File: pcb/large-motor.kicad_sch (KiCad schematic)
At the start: 15 parts, among them J6 Screw_Terminal_01x02, U27 DRV8874PWPR

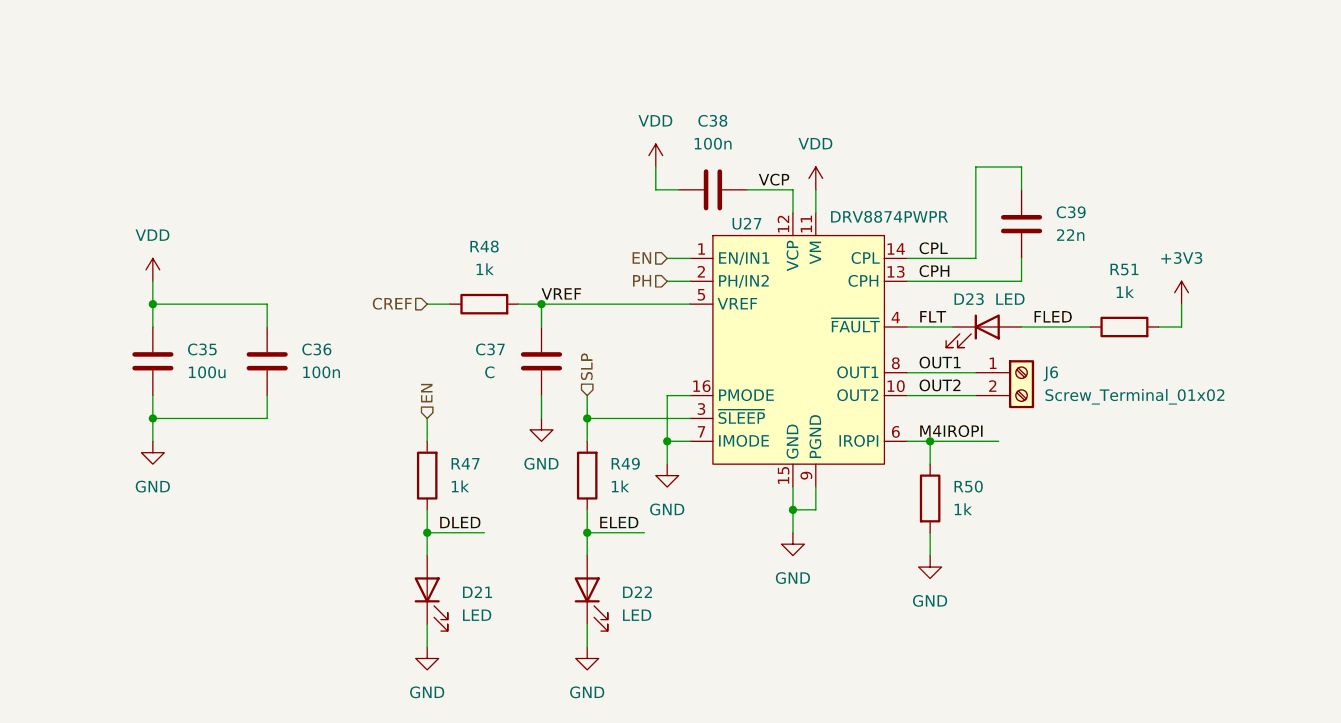
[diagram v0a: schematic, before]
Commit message: Remove sensor hub
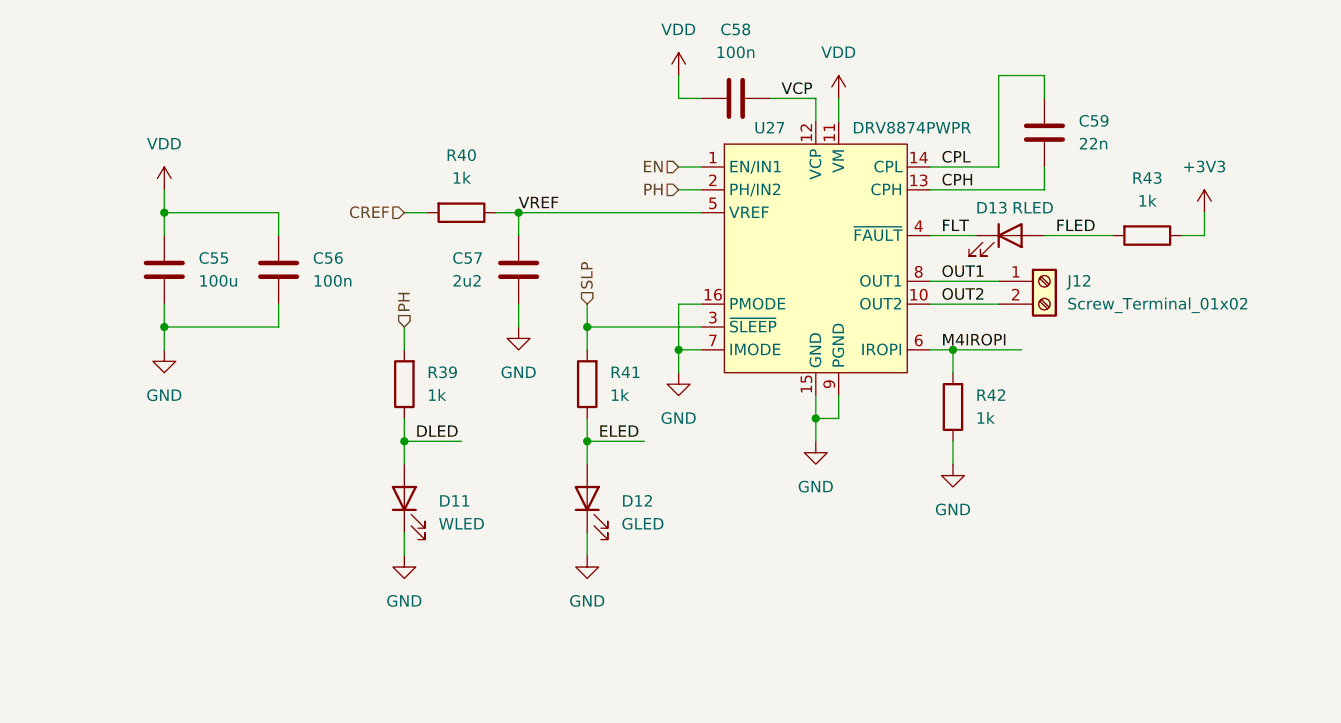
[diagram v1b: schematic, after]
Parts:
- removed R48, R49, R50, R51: 1k, symbol Device:R
- added R40, R41, R42, R43: 1k, Resistor_SMD:R_0402_1005Metric, symbol Device:R
- C57: renamed from C37; value C -> 2u2; LCSC (none) -> C12530
- C58: renamed from C38; LCSC (none) -> C307331
- C59: renamed from C39; LCSC (none) -> C1532
- D11: renamed from D21; value LED -> WLED; footprint (none) -> LED_SMD:LED_0603_1608Metric; LCSC (none) -> C2290
- D12: renamed from D22; value LED -> GLED; footprint (none) -> LED_SMD:LED_0603_1608Metric; LCSC (none) -> C72043
- D13: renamed from D23; value LED -> RLED; footprint (none) -> LED_SMD:LED_0603_1608Metric; LCSC (none) -> C2286
- J12: renamed from J6; footprint (none) -> TerminalBlock_Phoenix:TerminalBlock_Phoenix_MKDS-1,5-2_1x02_P5.00mm_Horizontal; LCSC (none) -> C8404
- R39: renamed from R47; footprint (none) -> Resistor_SMD:R_0402_1005Metric; LCSC (none) -> C11702
- U27: LCSC (none) -> C1855818
- renumbered C35 to C55, C36 to C56
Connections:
- net +3V3: now also R43.1
- net CREF: now also R40.2
- net ELED: now also R41.1
- net EN: no longer R39.2
- net FLED: now also R43.2
- net GND: now also R42.1
- net M4IROPI: now also R42.2
- net PH: now also R39.2
- net SLP: now also R41.2
- net VREF: now also R40.1
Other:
- moved on the sheet: C55, C56, C57, C58, C59, D11, D12, D13, J12, R39, U27

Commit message: Finish schematic
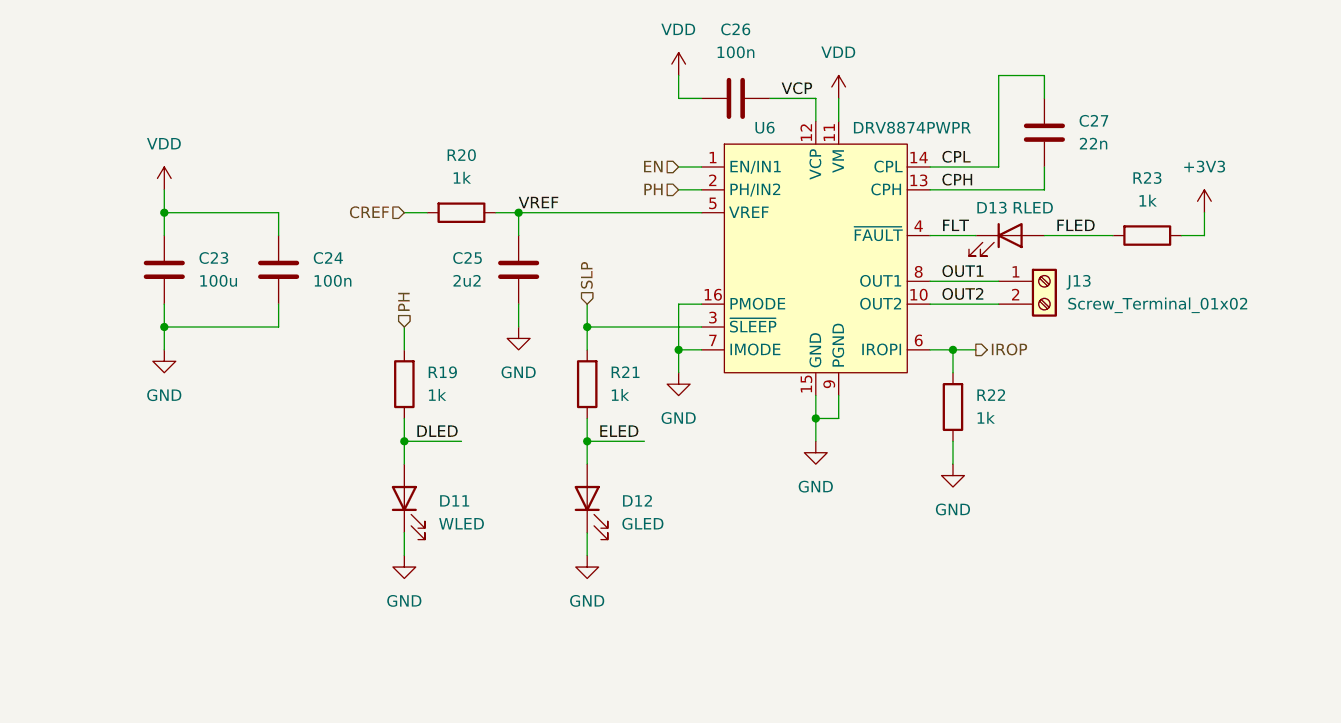
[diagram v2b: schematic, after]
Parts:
- renumbered C55 to C23, C56 to C24, C57 to C25, C58 to C26, C59 to C27, J12 to J13, R39 to R19, R40 to R20, R41 to R21, R42 to R22, R43 to R23, U27 to U6
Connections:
- net M4IROPI renamed IROP

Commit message: Save progress
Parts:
- removed C23: 100u, Capacitor_SMD:C_Elec_8x6.2, symbol Device:C
- removed J13: Screw_Terminal_01x02, TerminalBlock_Phoenix:TerminalBlock_Phoenix_MKDS-1,5-2_1x02_P5.00mm_Horizontal, symbol Connector:Screw_Terminal_01x02
- renumbered C24 to C66, C25 to C67, C26 to C68, C27 to C69, D11 to D26, D12 to D27, D13 to D28, R19 to R59, R20 to R60, R21 to R61, R22 to R62, R23 to R63, U6 to U30
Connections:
- net OUT1 renamed OUTA
- net OUT2 renamed OUTB

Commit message: Save progress
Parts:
- added C13, C57: 22u, Capacitor_SMD:C_0805_2012Metric, symbol Device:C
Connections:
- net GND: now also C13.2, C57.2
- net VDD: now also C13.1, C57.1

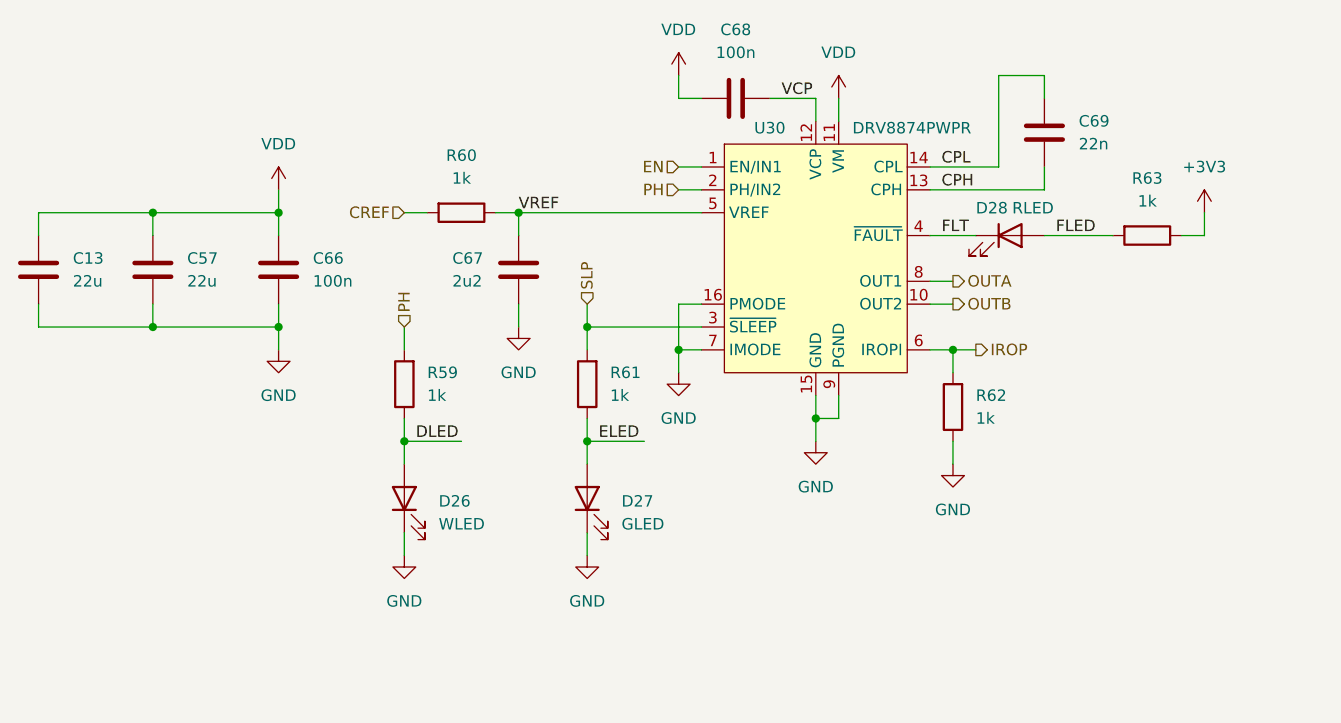
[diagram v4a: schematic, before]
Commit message: Finish schematic
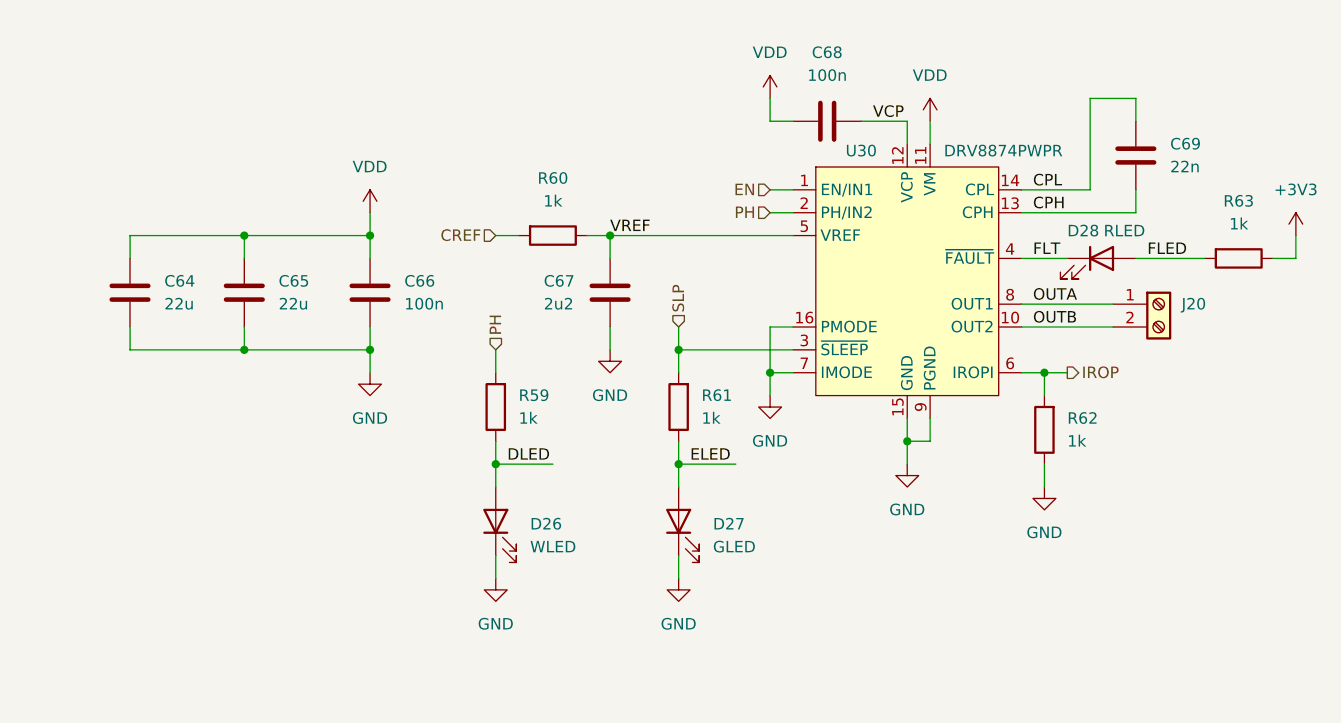
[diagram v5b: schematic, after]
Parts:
- added J20: Screw_Terminal_01x02, TerminalBlock_Phoenix:TerminalBlock_Phoenix_MKDS-1,5-2_1x02_P5.00mm_Horizontal, symbol Connector:Screw_Terminal_01x02
- renumbered C13 to C64, C57 to C65
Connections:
- net OUTA: now also J20.1 (Pin_1)
- net OUTB: now also J20.2 (Pin_2)
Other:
- moved on the sheet: C64, C65, C66, C67, C68, C69, D26, D27, D28, R59, R60, R61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

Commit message: Start wiring
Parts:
- renumbered J20 to J29
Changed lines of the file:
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@@
 		(dnp no)
 		(fields_autoplaced yes)
-		(property "Reference" "J20"
+		(property "Reference" "J29"
 			(at 152.4 58.4199 0)
 			(effects

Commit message: Add power switch
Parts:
- J29: now not fitted
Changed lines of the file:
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@@
 		(in_bom yes)
 		(on_board yes)
-		(dnp no)
+		(dnp yes)
 		(fields_autoplaced yes)
 		(property "Reference" "J29"

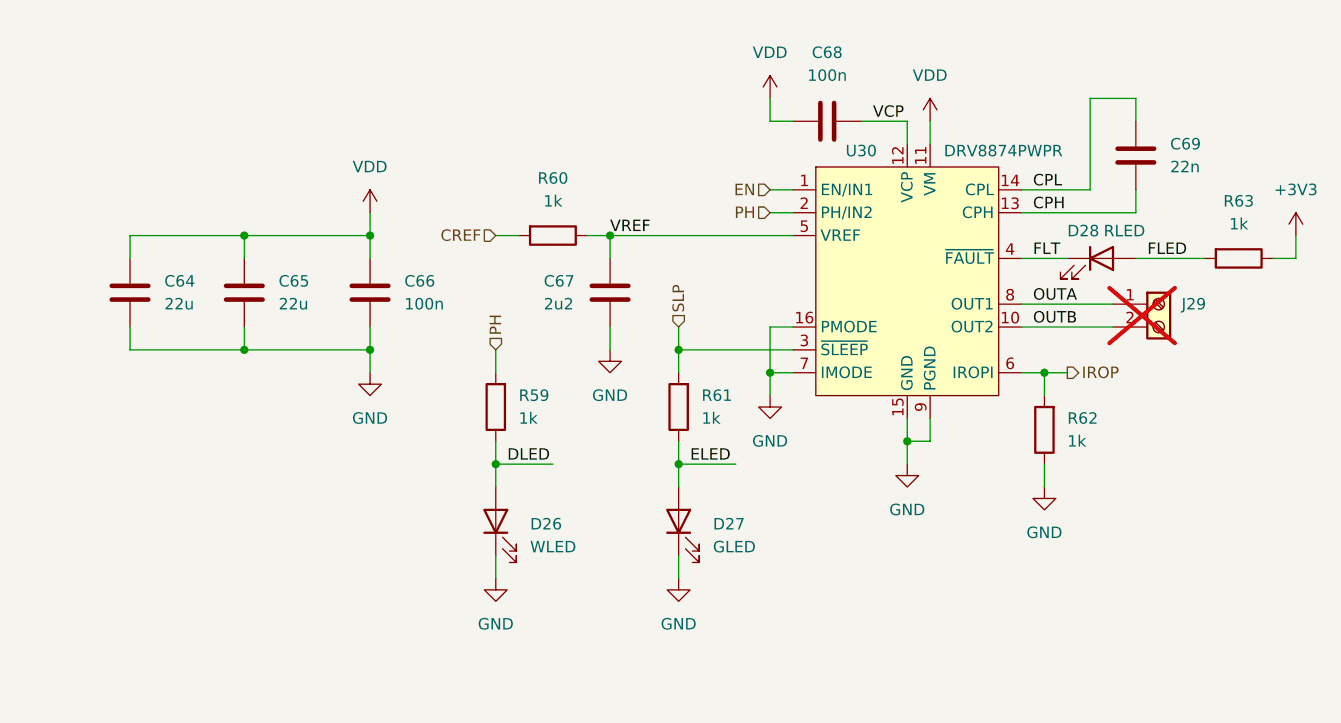
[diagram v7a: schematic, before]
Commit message: Fix encoder pull downs
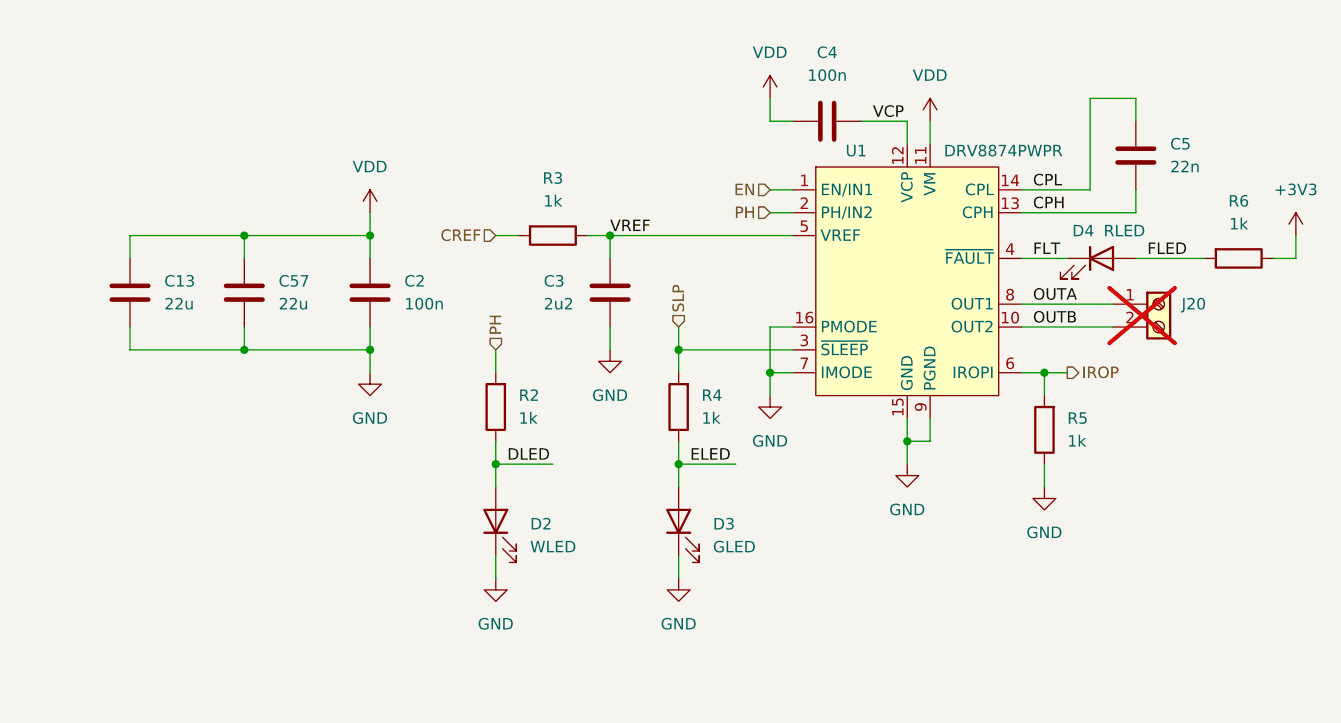
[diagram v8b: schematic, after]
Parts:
- renumbered C64 to C13, C66 to C2, C67 to C3, C68 to C4, C69 to C5, C65 to C57, D26 to D2, D27 to D3, D28 to D4, J29 to J20, R59 to R2, R60 to R3, R61 to R4, R62 to R5, R63 to R6, U30 to U1
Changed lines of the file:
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@@
 (kicad_sch
-	(version 20231120)
+	(version 20250114)
 	(generator "eeschema")
-	(generator_version "8.0")
+	(generator_version "9.0")
 	(paper "A5")
 	(junction
@@
 	(label "CPH"
 		(at 135.89 48.26 0)
-		(fields_autoplaced yes)
 		(effects
 			(font
@@
 	(label "OUTB"
 		(at 135.89 60.96 0)
-		(fields_autoplaced yes)
 		(effects
 			(font
@@
 	(label "CPL"
 		(at 135.89 45.72 0)
-		(fields_autoplaced yes)
 		(effects
 			(font
@@
 	(label "VCP"
 		(at 118.11 38.1 0)
-		(fields_autoplaced yes)
 		(effects
 			(font
@@
 	(label "OUTA"
 		(at 135.89 58.42 0)
-		(fields_autoplaced yes)
 		(effects
 			(font
@@
 	(label "FLED"
 		(at 148.59 53.34 0)
-		(fields_autoplaced yes)
 		(effects
 			(font
@@
 	(label "ELED"
 		(at 97.79 76.2 0)
-		(fields_autoplaced yes)
 		(effects
 			(font
@@
 	(label "VREF"
 		(at 88.9 50.8 0)
-		(fields_autoplaced yes)
 		(effects
 			(font
@@
 	(label "DLED"
 		(at 77.47 76.2 0)
-		(fields_autoplaced yes)
 		(effects
 			(font
@@
 	(label "FLT"
 		(at 135.89 53.34 0)
-		(fields_autoplaced yes)
 		(effects
 			(font
@@
 		(shape input)
 		(at 76.2 50.8 180)
-		(fields_autoplaced yes)
 		(effects
 			(font
@@
 		(shape input)
 		(at 96.52 60.96 90)
-		(fields_autoplaced yes)
 		(effects
 			(font
@@
 		(shape input)
 		(at 106.68 48.26 180)
-		(fields_autoplaced yes)
 		(effects
 			(font
@@
 		(shape input)
 		(at 106.68 45.72 180)
-		(fields_autoplaced yes)
 		(effects
 			(font
@@
 		(shape output)
 		(at 139.7 66.04 0)
-		(fields_autoplaced yes)
 		(effects
 			(font
@@
 		(shape input)
 		(at 76.2 63.5 90)
-		(fields_autoplaced yes)
 		(effects
 			(font
@@
 		(dnp no)
 		(fields_autoplaced yes)
-		(property "Reference" "D27"
+		(property "Reference" "D3"
 			(at 100.33 82.8674 90)
 			(effects
@@
 		(dnp no)
 		(fields_autoplaced yes)
-		(property "Reference" "R60"
+		(property "Reference" "R3"
 			(at 82.55 44.45 90)
 			(effects
@@
 		(dnp no)
 		(fields_autoplaced yes)
-		(property "Reference" "#PWR0242"
+		(property "Reference" "#PWR016"
 			(at 88.9 69.85 0)
 			(effects
@@
 		(on_board yes)
 		(dnp no)
-		(property "Reference" "D28"
+		(property "Reference" "D4"
 			(at 141.478 50.292 0)
 			(effects
@@
 		(dnp yes)
 		(fields_autoplaced yes)
-		(property "Reference" "J29"
+		(property "Reference" "J20"
 			(at 152.4 58.4199 0)
 			(effects
@@
 		(dnp no)
 		(fields_autoplaced yes)
-		(property "Reference" "R61"
+		(property "Reference" "R4"
 			(at 99.06 68.5799 0)
 			(effects
@@
 		(dnp no)
 		(fields_autoplaced yes)
-		(property "Reference" "#PWR0112"
+		(property "Reference" "#PWR013"
 			(at 62.23 52.07 0)
 			(effects
@@
 		(dnp no)
 		(fields_autoplaced yes)
-		(property "Reference" "C65"
+		(property "Reference" "C57"
 			(at 52.07 55.8799 0)
 			(effects
@@
 		(dnp no)
 		(fields_autoplaced yes)
-		(property "Reference" "#PWR0241"
+		(property "Reference" "#PWR015"
 			(at 76.2 95.25 0)
 			(effects
@@
 		(dnp no)
 		(fields_autoplaced yes)
-		(property "Reference" "#PWR0245"
+		(property "Reference" "#PWR019"
 			(at 106.68 74.93 0)
 			(effects
@@
 		(dnp no)
 		(fields_autoplaced yes)
-		(property "Reference" "D26"
+		(property "Reference" "D2"
 			(at 80.01 82.8674 90)
 			(effects
@@
 		(dnp no)
 		(fields_autoplaced yes)
-		(property "Reference" "R63"
+		(property "Reference" "R6"
 			(at 158.75 46.99 90)
 			(effects
@@
 		(dnp no)
 		(fields_autoplaced yes)
-		(property "Reference" "C64"
+		(property "Reference" "C13"
 			(at 39.37 55.8799 0)
 			(effects
@@
 		(dnp no)
 		(fields_autoplaced yes)
-		(property "Reference" "R62"
+		(property "Reference" "R5"
 			(at 139.7 71.1199 0)
 			(effects
@@
 		(dnp no)
 		(fields_autoplaced yes)
-		(property "Reference" "C69"
+		(property "Reference" "C5"
 			(at 151.13 40.64 0)
 			(effects
@@
 		(dnp no)
 		(fields_autoplaced yes)
-		(property "Reference" "#PWR0248"
+		(property "Reference" "#PWR022"
 			(at 137.16 85.09 0)
 			(effects
@@
 		(dnp no)
 		(fields_autoplaced yes)
-		(property "Reference" "C68"
+		(property "Reference" "C4"
 			(at 113.03 30.48 90)
 			(effects
@@
 		(on_board yes)
 		(dnp no)
-		(property "Reference" "C67"
+		(property "Reference" "C3"
 			(at 81.534 55.88 0)
 			(effects
@@
 		(on_board yes)
 		(dnp no)
-		(property "Reference" "U30"
+		(property "Reference" "U1"
 			(at 115.062 41.402 0)
 			(effects
@@
 		(dnp no)
 		(fields_autoplaced yes)
-		(property "Reference" "#PWR0116"
+		(property "Reference" "#PWR014"
 			(at 62.23 72.39 0)
 			(effects
@@
 		(dnp no)
 		(fields_autoplaced yes)
-		(property "Reference" "#PWR0249"
+		(property "Reference" "#PWR023"
 			(at 165.1 54.61 0)
 			(effects
@@
 		(dnp no)
 		(fields_autoplaced yes)
-		(property "Reference" "R59"
+		(property "Reference" "R2"
 			(at 78.74 68.5799 0)
 			(effects
@@
 		(dnp no)
 		(fields_autoplaced yes)
-		(property "Reference" "C66"
+		(property "Reference" "C2"
 			(at 66.04 55.88 0)
 			(effects
@@
 		(dnp no)
 		(fields_autoplaced yes)
-		(property "Reference" "#PWR0246"
+		(property "Reference" "#PWR020"
 			(at 121.92 82.55 0)
 			(effects
@@
 		(dnp no)
 		(fields_autoplaced yes)
-		(property "Reference" "#PWR0247"
+		(property "Reference" "#PWR021"
 			(at 124.46 41.91 0)
 			(effects
@@
 		(dnp no)
 		(fields_autoplaced yes)
-		(property "Reference" "#PWR0244"
+		(property "Reference" "#PWR018"
 			(at 106.68 39.37 0)
 			(effects
@@
 		(dnp no)
 		(fields_autoplaced yes)
-		(property "Reference" "#PWR0243"
+		(property "Reference" "#PWR017"
 			(at 96.52 95.25 0)
 			(effects
